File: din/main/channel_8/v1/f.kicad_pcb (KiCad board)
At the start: 2 copper layers, 76.8 x 81.3 mm, 40 parts, among them J1 fm16_i, J19 wrs_i, J2 Bus88_2x14, J3 selector4_i, U1 LTV-357T, U2 LTV-357T, U3 74LS245, U4 LTV-357T, U5 LTV-357T, U6 LTV-357T, U7 LTV-357T, U8 LTV-357T, U9 LTV-357T

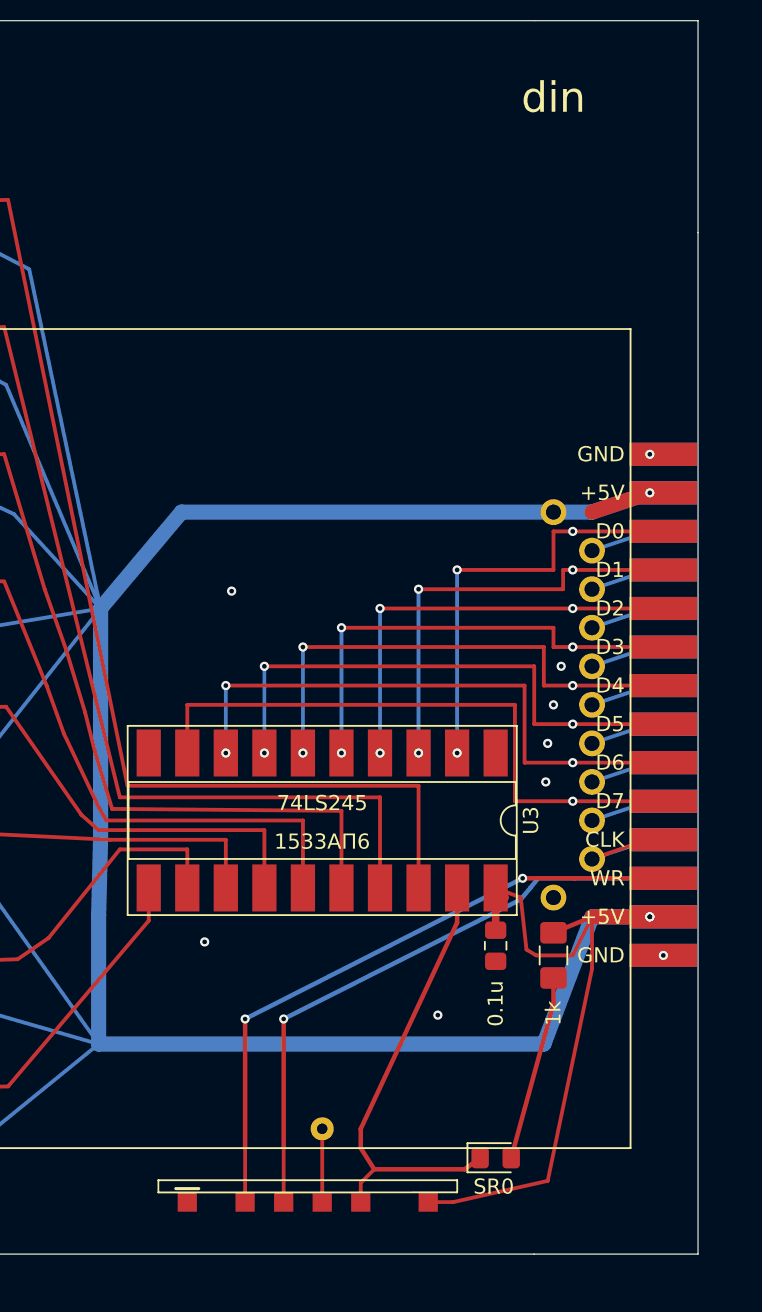
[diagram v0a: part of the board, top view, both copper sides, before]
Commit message: voltage regulator for each module
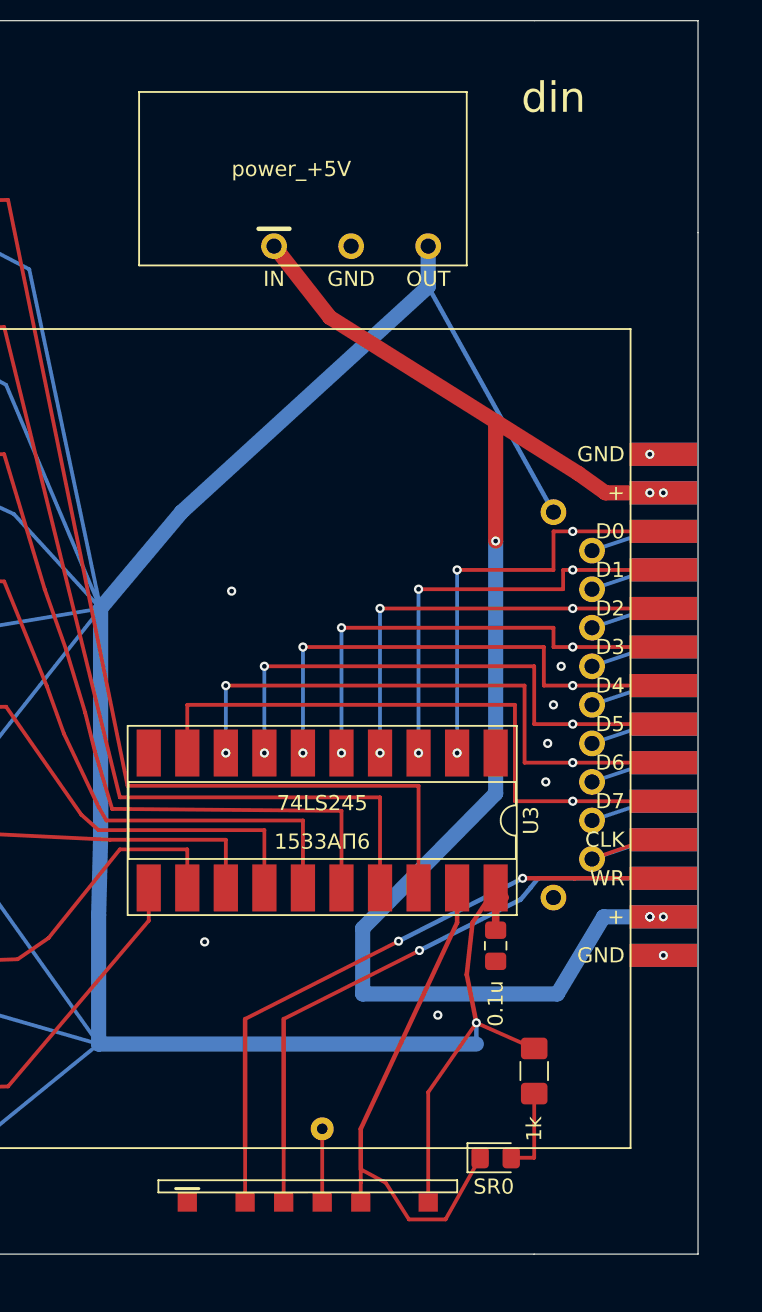
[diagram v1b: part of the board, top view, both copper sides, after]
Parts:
- added J4: power_+5V, plc88:power_i, F.Cu at (76.8, 35.2)
- J2: value Bus88_2x14 -> bus_i; footprint 1my_elements:Bus88_2x14 -> plc88:bus_im
- moved R17 7.73 mm to (100.3, 99.7)
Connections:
- J2 pad 25: +5V -> VPBUS
- J2 pad 26: +5V -> VPBUS
- J2 pad 3: +5V -> VPBUS
- J2 pad 4: +5V -> VPBUS
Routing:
- net VPBUS: track 0.00 -> 95.3 mm, vias 0 -> 6
- net +5V: track 268.2 -> 241.9 mm, vias 11 -> 9
- net Net-(D1-Pad2): track 12.2 -> 5.74 mm
- net SR0: track 30.0 -> 33.9 mm
